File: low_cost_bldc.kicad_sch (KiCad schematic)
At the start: 0 parts

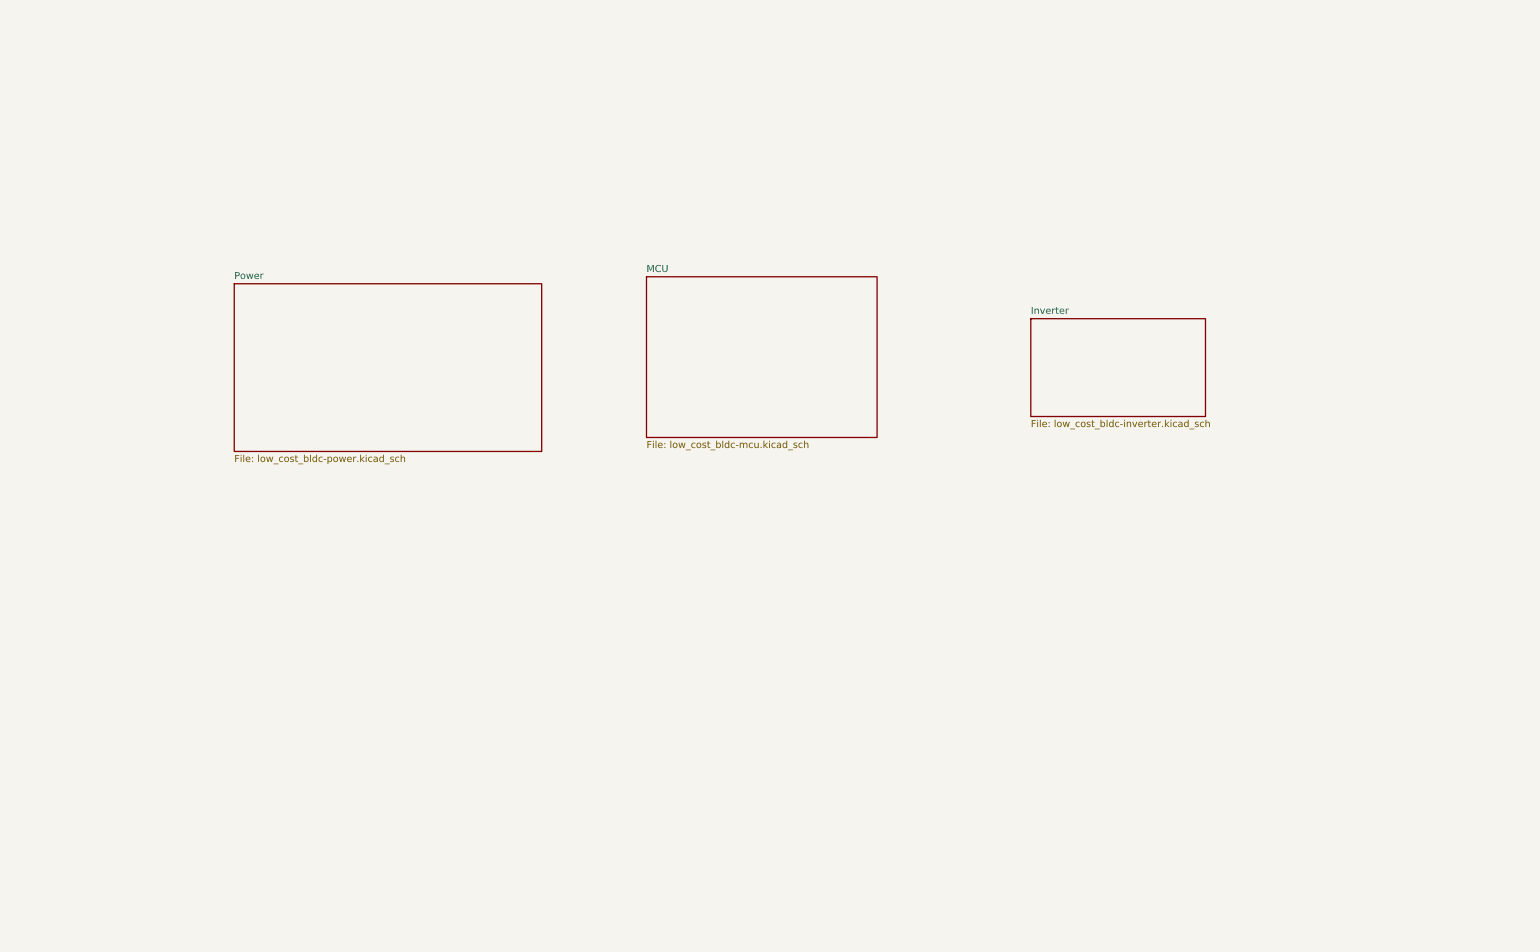
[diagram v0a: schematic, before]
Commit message: Top-only inverter layout
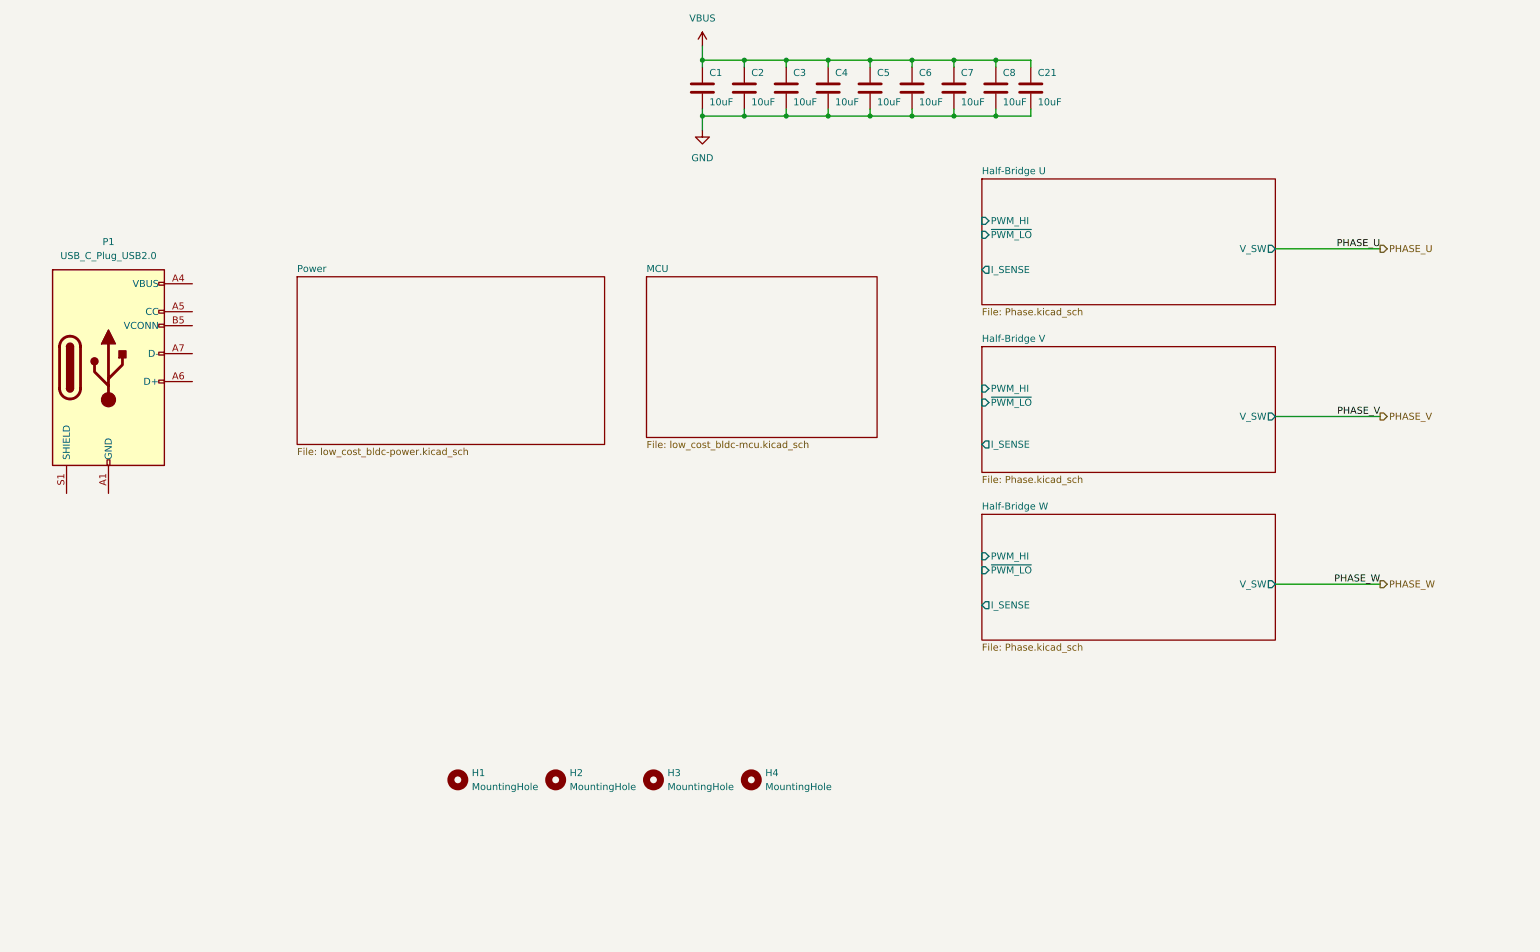
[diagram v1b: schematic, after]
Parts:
- added C1, C2, C21, C3, C4, C5, C6, C7, C8: 10uF, Capacitor_SMD:C_1206_3216Metric, symbol Device:C
- added H1, H2, H3, H4: MountingHole, MountingHole:MountingHole_3.2mm_M3, symbol Mechanical:MountingHole
- added P1: USB_C_Plug_USB2.0, Connector_USB:USB_C_Receptacle_Amphenol_12401610E4-2A, symbol Connector:USB_C_Plug_USB2.0
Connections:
- new net: P1.A1 (GND), P1.A12 (GND), P1.B1 (GND), P1.B12 (GND)
- new net: P1.A4 (VBUS), P1.A9 (VBUS), P1.B4 (VBUS), P1.B9 (VBUS)
- new net GND: C1.2, C2.2, C21.2, C3.2, C4.2, C5.2, C6.2, C7.2, C8.2
- new net VBUS: C1.1, C2.1, C21.1, C3.1, C4.1, C5.1, C6.1, C7.1, C8.1
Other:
- removed sheet Inverter
- added sheet Half-Bridge U (Phase.kicad_sch)
- added sheet Half-Bridge V (Phase.kicad_sch)
- added sheet Half-Bridge W (Phase.kicad_sch)
- title: (none) -> FreeWheel

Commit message: Initial mounting holes, power lugs. Sitting at  @ qty 10 BOM estimate. Still need 12V, 3.3V power; comms connectors
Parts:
- added H5, H6, H7, H8, H9: MountingHole_Pad, TestPoint:TestPoint_Plated_Hole_D2.0mm, symbol Mechanical:MountingHole_Pad
- added U9: IP2721, Package_SO:TSSOP-16_4.4x5mm_P0.65mm, symbol Interface_USB:IP2721
- H1, H2, H3, H4: footprint MountingHole:MountingHole_3.2mm_M3 -> MountingHole:MountingHole_2.7mm_M2.5
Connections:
- net GND: now also H8.1
- net PHASE_U: now also H5.1
- net PHASE_V: now also H6.1
- net PHASE_W: now also H7.1
- net VBUS: now also H9.1

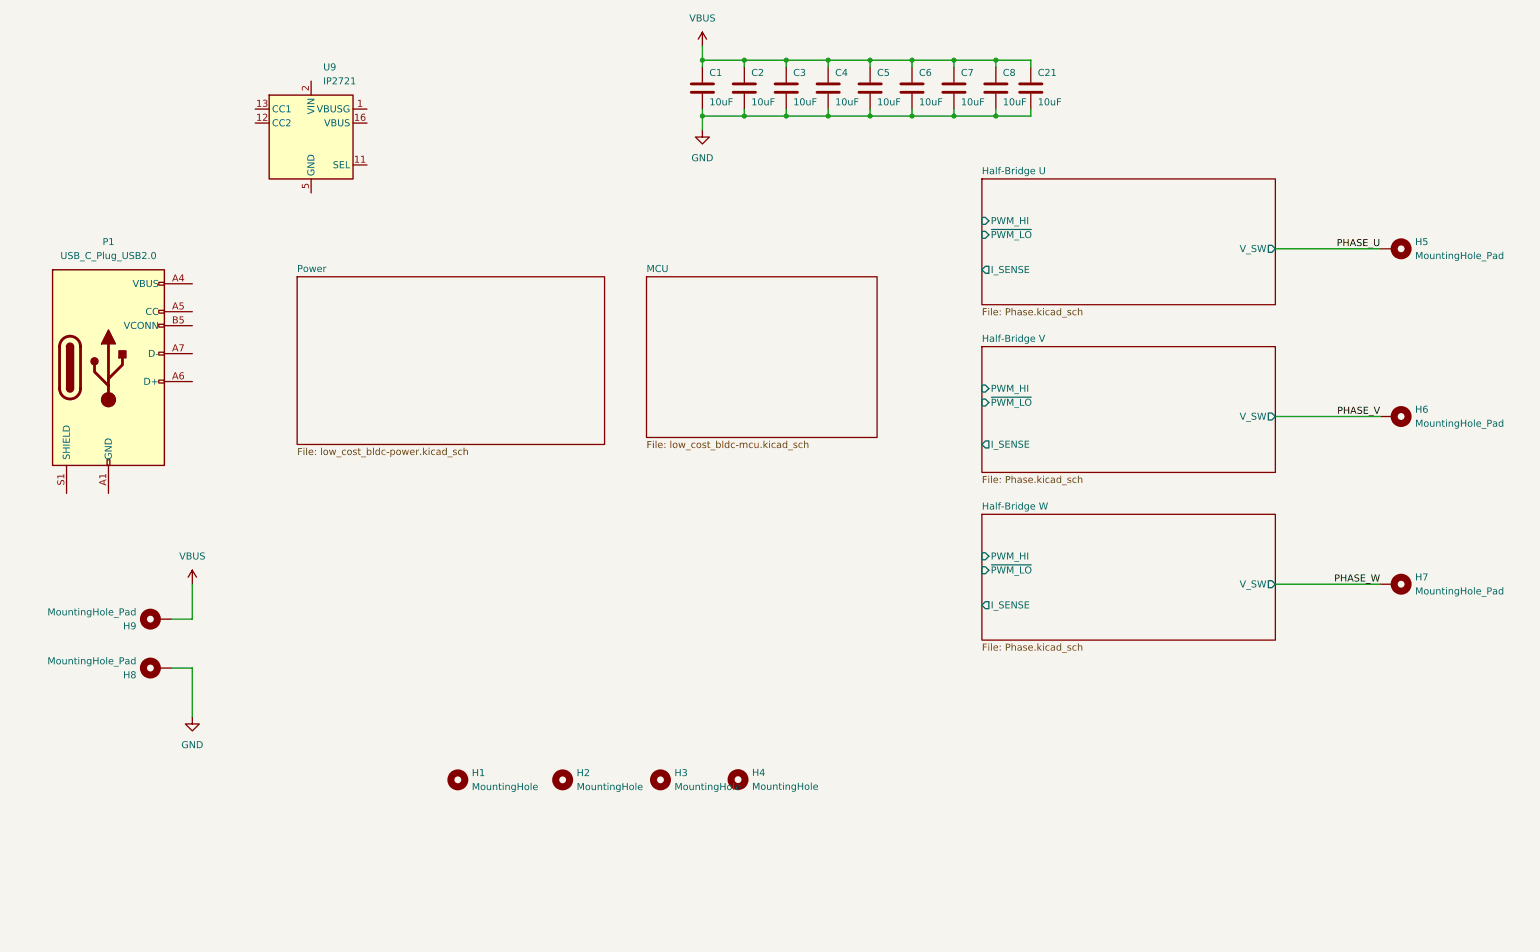
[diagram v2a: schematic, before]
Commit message: Readme, rough connector placement, inverter refinement, increase MCU pin count to have a chance of succeeding.
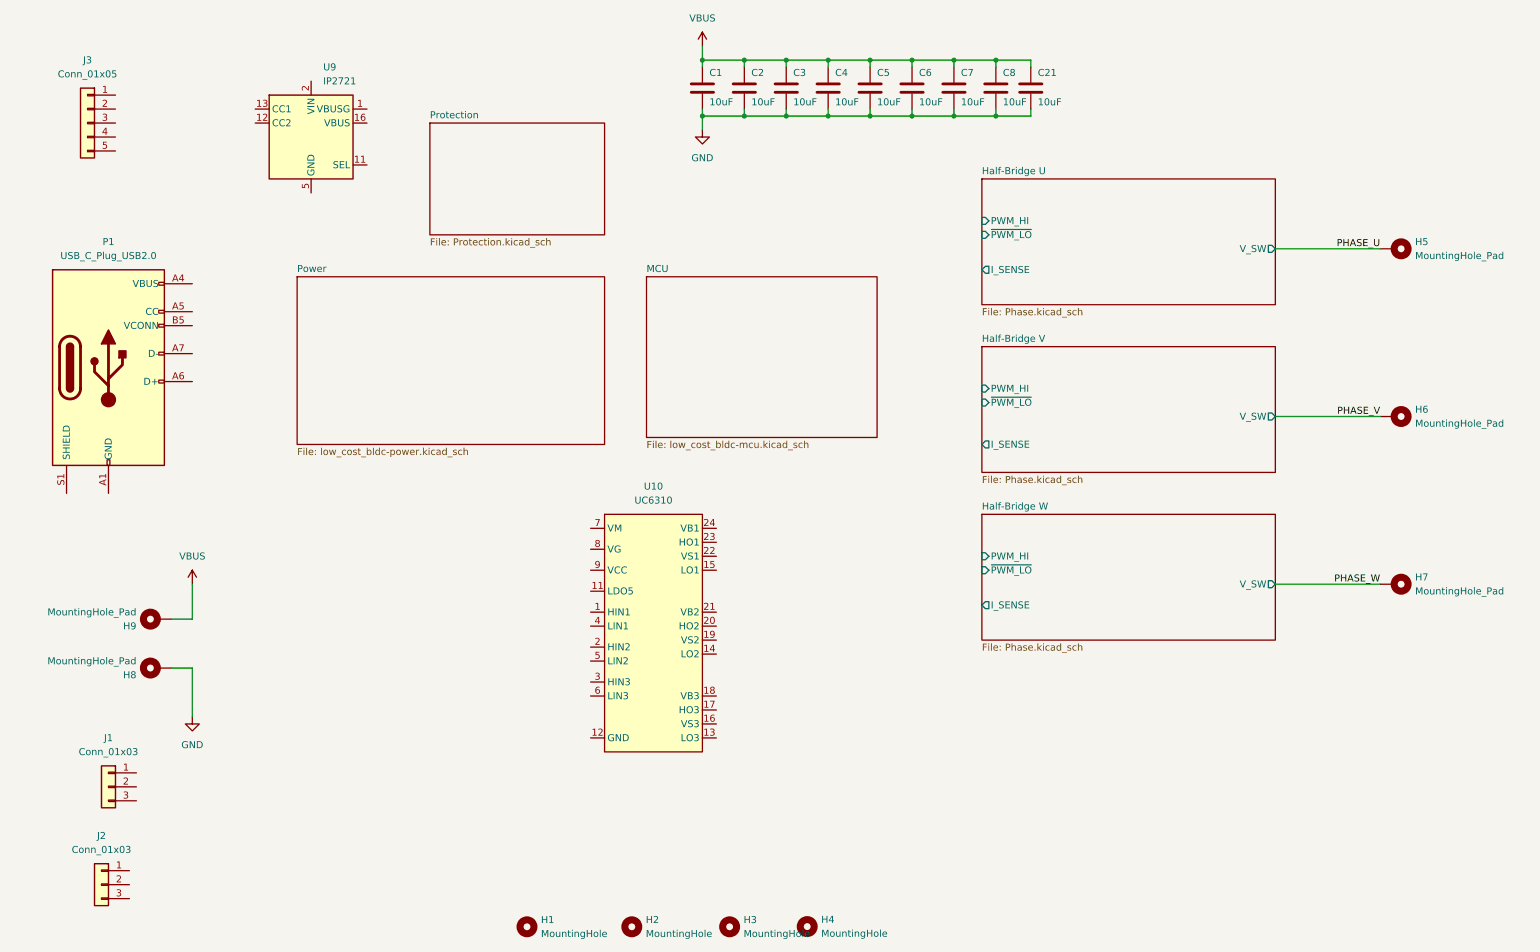
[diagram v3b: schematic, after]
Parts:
- added J1, J2: Conn_01x03, Connector_JST:JST_PH_B3B-PH-K_1x03_P2.00mm_Vertical, symbol Connector_Generic:Conn_01x03
- added J3: Conn_01x05, Connector_JST:JST_PH_B5B-PH-K_1x05_P2.00mm_Vertical, symbol Connector_Generic:Conn_01x05
- added U10: UC6310, Package_SO:SSOP-24_3.9x8.7mm_P0.635mm, symbol FreeWheel:U6310
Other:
- added sheet Protection (Protection.kicad_sch)
- moved on the sheet: H1, H2, H3, H4

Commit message: Organizing
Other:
- note added: "Sensor input or control input?"
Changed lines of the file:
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@@
+		)
+	)
+	(text "Sensor input or control input?"
+		(exclude_from_sim no)
+		(at 28.448 55.372 0)
+		(effects
+			(font
+				(size 1.27 1.27)
+			)
 		)
 	)
